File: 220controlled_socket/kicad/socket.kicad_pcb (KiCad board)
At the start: 2 copper layers, 71 parts, among them J1 DB9_Female, J2 USB_B, J3 5Vext, J4 SWIM, J5 DB15_Male, J6 Power, J7 Power, K1 SRD-05VDC, K2 SRD-05VDC, Q1 2N7002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

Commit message: 220v socket schematic is over
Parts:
- added REF**: VIA, my_footprints:VIA, F.Cu at (68.6, 73.7)
- added REF**: VIA, my_footprints:VIA, F.Cu at (57.1, 88.0)
- added REF**: VIA, my_footprints:VIA, F.Cu at (50.2, 58.3)
- C11, D5, Q6, Q8, Q9, R10, R14, R16, R18, R20, R22, R9, U10, U6, U7: moved to B.Cu
- C12: footprint Capacitor_SMD:C_0805_2012Metric_Pad1.15x1.50mm_HandSolder -> Capacitor_SMD:C_0603_1608Metric_Pad0.84x1.00mm_HandSolder; moved to B.Cu
- R15, R17: value 100 -> 150
- R19, R21: footprint Resistor_SMD:R_1206_3216Metric_Pad1.24x1.80mm_HandSolder -> Resistor_THT:R_Axial_DIN0309_L9.0mm_D3.2mm_P12.70mm_Horizontal
- R24: footprint Resistor_SMD:R_0603_1608Metric_Pad0.84x1.00mm_HandSolder -> Resistor_SMD:R_0805_2012Metric_Pad1.15x1.50mm_HandSolder
- REF** (x4): footprint MountingHole:MountingHole_3.2mm_M3 -> my_footprints:Hole_3mm
- moved C6 181.8 mm to (54.7, 62.4)
- moved R15 174.8 mm to (64.9, 25.1), turned to 180 degrees
- moved R8 173.2 mm to (68.2, 88.5), turned to 90 degrees
- moved R18 166.5 mm to (77.1, 53.4), turned to 180 degrees
- moved R16 166.3 mm to (81.7, 28.2), turned to 180 degrees
- moved Q2 161.7 mm to (61.5, 87.0)
- moved R3 156.8 mm to (61.0, 83.8)
- moved U6 154.9 mm to (66.0, 82.9)
- moved U5 151.5 mm to (78.9, 84.5), turned to 90 degrees
- moved Q1 150.1 mm to (67.6, 76.6), turned to 180 degrees
- moved Q8 149.7 mm to (87.0, 27.4)
- moved R5 149.4 mm to (57.3, 36.6), turned to 270 degrees
- moved R10 145.4 mm to (79.2, 87.4), turned to 180 degrees
- moved R17 145.2 mm to (77.1, 53.5), turned to 180 degrees
- moved Q4 144.6 mm to (94.1, 84.6)
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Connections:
- K1 pad 2: Net-(K1-Pad2) -> VCC
- K1 pad 3: (no net) -> Net-(D3-Pad1)
- K1 pad 4: Net-(D3-Pad1) -> (no net)
- K1 pad 5: VCC -> Net-(K1-Pad5)
- K2 pad 2: Net-(K2-Pad2) -> VCC
- K2 pad 3: (no net) -> Net-(D4-Pad1)
- K2 pad 4: Net-(D4-Pad1) -> (no net)
- K2 pad 5: VCC -> Net-(K2-Pad5)
- Q8 pad 3: Net-(K1-Pad2) -> Net-(K1-Pad5)
- Q9 pad 3: Net-(K2-Pad2) -> Net-(K2-Pad5)
- R10 pad 1: Net-(J5-Pad10) -> Net-(J5-Pad9)
- U10 pad 1: Net-(J6-Pad3) -> Net-(D3-Pad1)
- U10 pad 2: Net-(J6-Pad3) -> Net-(D3-Pad1)
- U10 pad 3: Net-(D3-Pad1) -> Net-(J6-Pad3)
- U10 pad 4: Net-(D3-Pad1) -> Net-(J6-Pad3)
- U3 pad 10: /PKEY1 -> /Out0
- U3 pad 11: /Out1 -> /PKEY1
- U3 pad 12: /Out0 -> /~In0
- U3 pad 14: Net-(C13-Pad1) -> /Relay1
- U3 pad 16: /Relay1 -> /Triac1
- U3 pad 17: /Triac1 -> /Relay0
- U3 pad 19: /Relay0 -> /Triac0
- U3 pad 20: /Triac0 -> Net-(C13-Pad1)
- U3 pad 5: /~In0 -> /~In1
- U3 pad 6: /~In1 -> /Out1
- U5 pad 2: Net-(J5-Pad9) -> Net-(J5-Pad10)
- U5 pad 3: GND -> /~In1
- U5 pad 4: /~In1 -> GND
- U6 pad 3: Net-(J5-Pad3) -> Net-(J5-Pad4)
- U6 pad 4: Net-(J5-Pad4) -> Net-(J5-Pad3)
- U7 pad 3: Net-(J5-Pad1) -> Net-(J5-Pad2)
- U7 pad 4: Net-(J5-Pad2) -> Net-(J5-Pad1)
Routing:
- net GND: track 21.9 -> 513.2 mm, vias 0 -> 5
- net VCC: track 16.0 -> 197.0 mm, vias 0 -> 2
- net /NKEY2: track 0.00 -> 65.0 mm
- net /NKEY1: track 0.00 -> 63.7 mm
- net /PKEY1: track 0.00 -> 62.7 mm, vias 0 -> 1
- net /Cur0: track 0.00 -> 60.9 mm, vias 0 -> 1
- net /~In0: track 6.73 -> 63.1 mm, vias 0 -> 1
- net /Out0: track 0.00 -> 48.4 mm
- net /~In1: track 5.73 -> 53.4 mm, vias 0 -> 1
- net GNDREF: track 0.00 -> 46.8 mm
- net Net-(R17-Pad1): track 0.00 -> 45.2 mm, vias 0 -> 1
- net Net-(D4-Pad1): track 0.00 -> 44.5 mm
- net /Out1: track 0.00 -> 42.9 mm
- net Net-(D3-Pad2): track 0.00 -> 42.8 mm
- net Net-(R15-Pad1): track 0.00 -> 40.5 mm, vias 0 -> 1
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- added copper zone on B.Cu, net GND
- added copper zone on F.Cu, net GND
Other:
- board outline added: 87 x 71 mm

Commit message: fix error in U5 connection on 220v socket
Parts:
- U5: moved to B.Cu
- moved U5 2.54 mm to (81.4, 84.5)
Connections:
- U5 pad 1: Net-(R10-Pad2) -> Net-(J5-Pad10)
- U5 pad 2: Net-(J5-Pad10) -> Net-(R10-Pad2)
- U5 pad 3: /~In1 -> GND
- U5 pad 4: GND -> /~In1
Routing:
- net GND: track 513.2 -> 518.8 mm

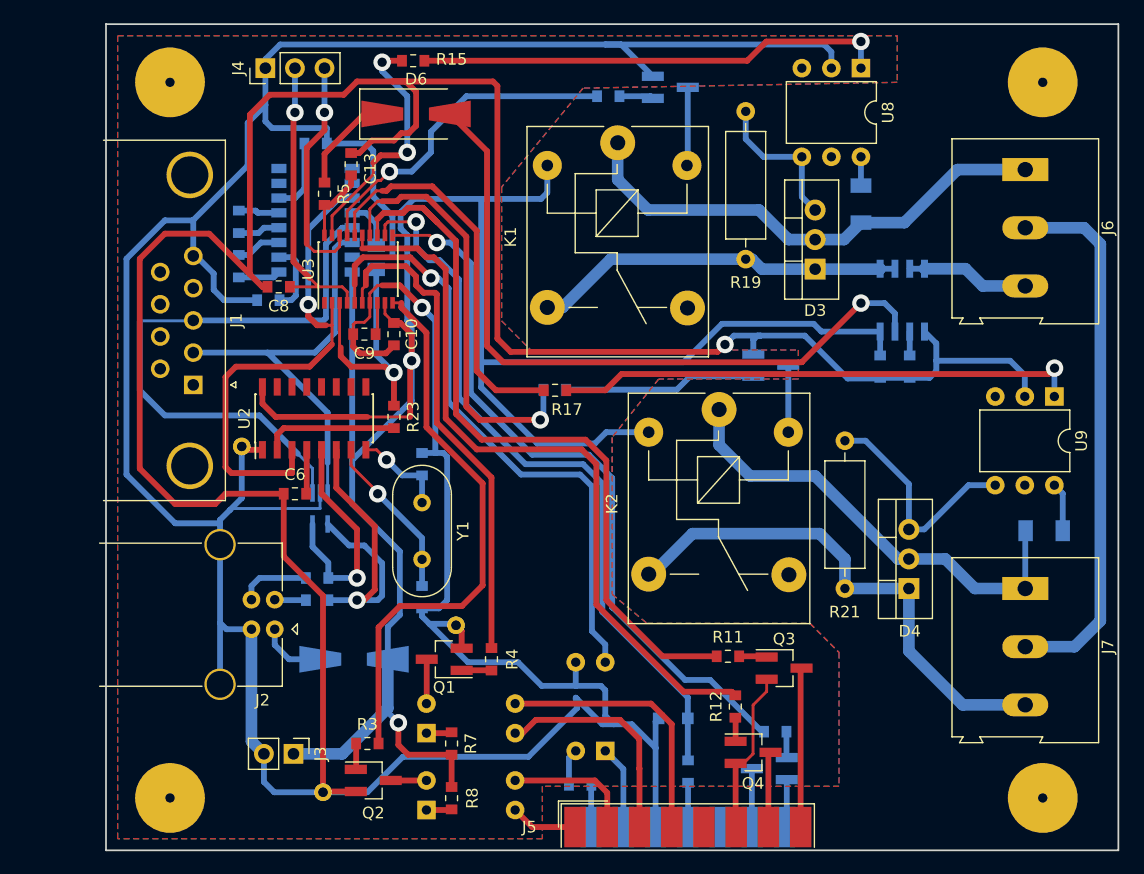
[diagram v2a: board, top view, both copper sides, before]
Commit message: fix bugs in 220v socket schematics
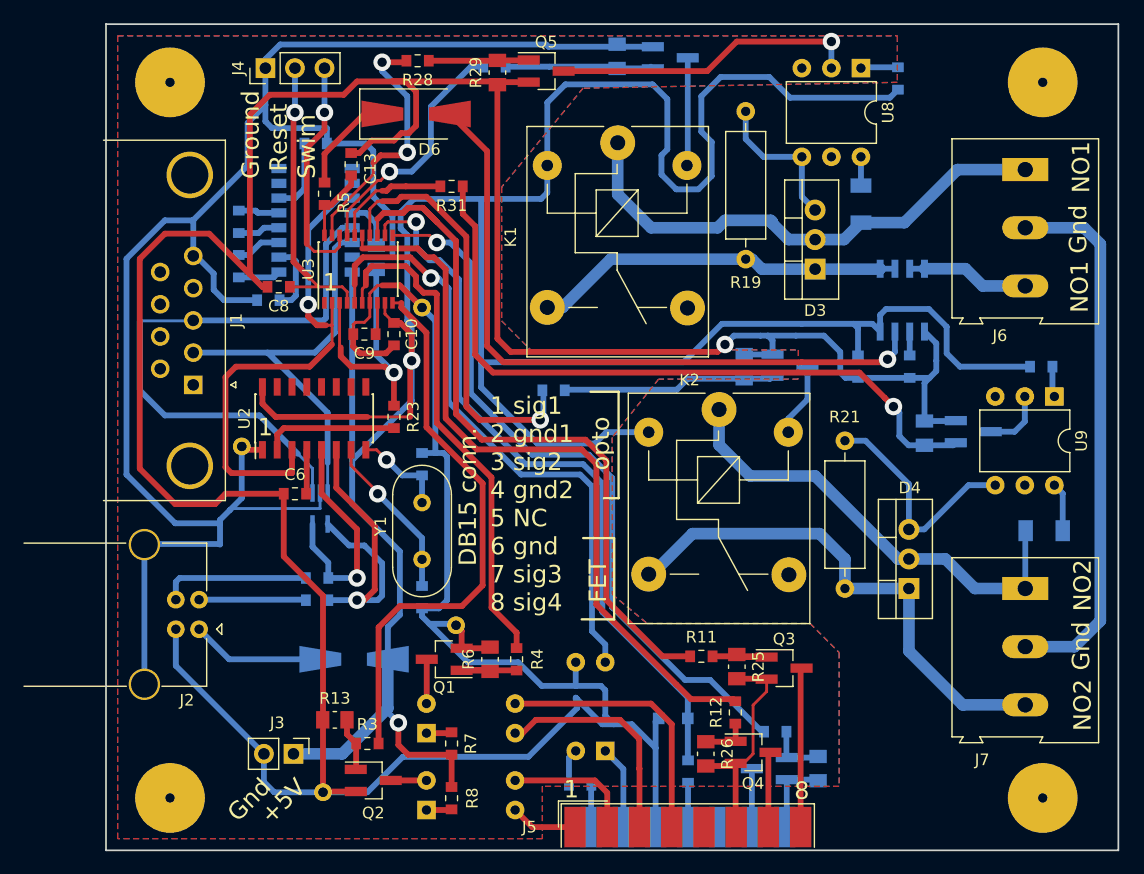
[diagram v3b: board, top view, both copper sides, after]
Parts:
- added Q5: 2N7002, Package_TO_SOT_SMD:SOT-23_Handsoldering, F.Cu at (76.3, 26.0)
- added Q7: 2N7002, Package_TO_SOT_SMD:SOT-23_Handsoldering, B.Cu at (113.0, 57.0)
- added R13: 47k, Resistor_SMD:R_0805_2012Metric_Pad1.15x1.50mm_HandSolder, F.Cu at (58.2, 81.8)
- added R25: 47k, Resistor_SMD:R_0805_2012Metric_Pad1.15x1.50mm_HandSolder, F.Cu at (92.7, 77.2)
- added R26: 47k, Resistor_SMD:R_0805_2012Metric_Pad1.15x1.50mm_HandSolder, F.Cu at (90.0, 84.7)
- added R27: 47k, Resistor_SMD:R_0805_2012Metric_Pad1.15x1.50mm_HandSolder, B.Cu at (99.7, 86.0)
- added R28: 330, Resistor_SMD:R_0603_1608Metric_Pad0.84x1.00mm_HandSolder, F.Cu at (65.3, 25.1)
- added R29: 47k, Resistor_SMD:R_0805_2012Metric_Pad1.15x1.50mm_HandSolder, F.Cu at (72.1, 26.2)
- added R30: 47k, Resistor_SMD:R_0805_2012Metric_Pad1.15x1.50mm_HandSolder, B.Cu at (82.4, 24.8)
- added R31: 330, Resistor_SMD:R_0603_1608Metric_Pad0.84x1.00mm_HandSolder, F.Cu at (68.2, 35.9)
- added R32: 47k, Resistor_SMD:R_0805_2012Metric_Pad1.15x1.50mm_HandSolder, B.Cu at (108.8, 57.1)
- added R33: 47k, Resistor_SMD:R_0805_2012Metric_Pad1.15x1.50mm_HandSolder, B.Cu at (93.3, 51.4)
- added R6: 47k, Resistor_SMD:R_0805_2012Metric_Pad1.15x1.50mm_HandSolder, F.Cu at (71.5, 76.6)
- added REF**: VIA, my_footprints:VIA, F.Cu at (65.7, 46.4)
- R15, R17: moved to B.Cu
- moved R17 41.8 mm to (118.9, 51.4)
- moved R15 41.7 mm to (106.6, 26.7), turned to 270 degrees
- moved R16 10.1 mm to (71.9, 25.7)
- moved J2 6.50 mm to (46.5, 74.0)
- moved Q8 2.54 mm to (87.0, 24.9)
- moved R11 2.29 mm to (89.7, 76.3)
- moved R4 2.16 mm to (73.8, 76.6)
- moved C11 1.91 mm to (103.1, 51.4)
- moved Q9 1.65 mm to (97.3, 51.3)
- moved R12 0.51 mm to (92.6, 81.2)
- moved R18 0.10 mm to (77.0, 53.5)
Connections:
- J5 pad 6: Net-(J5-Pad6) -> GND
- Q3 pad 2: Net-(J5-Pad6) -> GND
- Q4 pad 2: Net-(J5-Pad6) -> GND
- R15 pad 2: /Triac0 -> VCC
- R17 pad 2: /Triac1 -> VCC
- U8 pad 2: GND -> Net-(Q5-Pad3)
- U9 pad 2: GND -> Net-(Q7-Pad3)
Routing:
- net VCC: track 197.0 -> 270.7 mm
- net Net-(Q7-Pad1): track 0.00 -> 60.7 mm, vias 0 -> 1
- net Net-(R17-Pad1): track 45.2 -> 2.63 mm, vias 1 -> 0
- net Net-(R15-Pad1): track 40.5 -> 3.21 mm, vias 1 -> 0
- net Net-(Q5-Pad3): track 0.00 -> 26.3 mm, vias 0 -> 1
- net /Triac1: track 33.5 -> 10.3 mm
- net Net-(J5-Pad6): track 14.2 -> 0.00 mm
- net Net-(Q8-Pad1): track 2.95 -> 13.0 mm
- net GND: track 518.8 -> 527.6 mm
- net Net-(Q5-Pad1): track 0.00 -> 8.61 mm
- net /Relay0: track 28.7 -> 21.2 mm
- net Net-(J2-Pad3): track 6.14 -> 12.8 mm
- net Net-(J2-Pad2): track 2.70 -> 9.20 mm
- net Net-(D2-Pad2): track 5.78 -> 11.5 mm
- net Net-(Q7-Pad3): track 0.00 -> 5.44 mm
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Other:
- board text added: "+5V"
- board text added: "1"
- board text added: "1 sig1 2 gnd1 3 sig2 4 gnd2 5 NC 6 gnd 7 sig3 8 sig4"
- board text added: "15"
- board text added: "8"
- board text added: "9"
- board text added: "9 +5v1 10 gnd1 11 gnd 12 3..5V log.in 13 NC 14 gnd2 15 3..15V"
- board text added: "DB15 conn."
- board text added: "FET"
- board text added: "Gnd"
- board text added: "Ground"
- board text added: "NO1"
- board text added: "NO2"
- board text added: "PMOS"
- board text added: "Reset"
- board text added: "Swim"
- board text added: "opto"

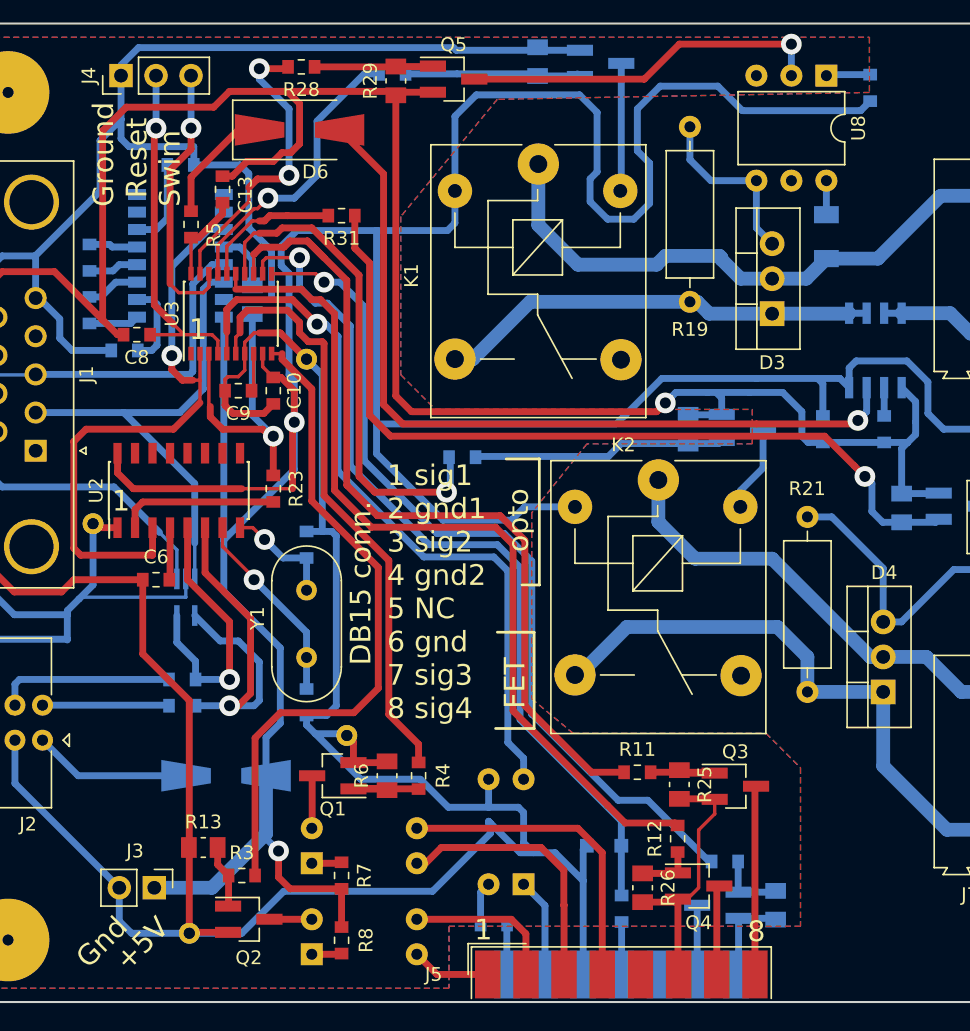
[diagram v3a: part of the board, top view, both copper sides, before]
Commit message: fix bug in max3232 & ch340 connection
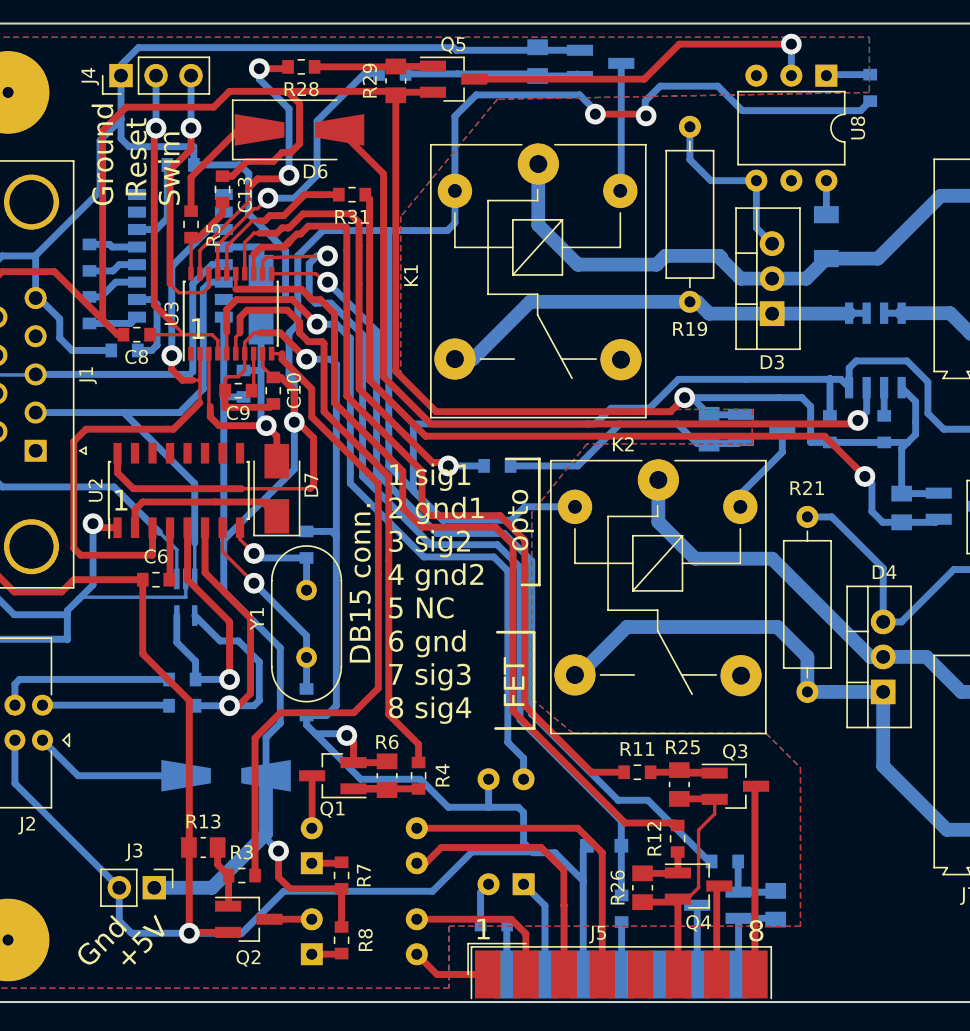
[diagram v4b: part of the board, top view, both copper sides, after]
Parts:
- removed R24: 510, Resistor_SMD:R_0805_2012Metric_Pad1.15x1.50mm_HandSolder
- removed the REF** at (65.7, 46.4)
- removed the REF** at (57.1, 88.0)
- removed the REF** at (50.2, 58.3)
- removed the REF** at (68.6, 73.7)
- added D7: SS14, Diode_SMD:D_SMA, F.Cu at (63.5, 55.8)
- added D8: SS14, Diode_SMD:D_SMA, B.Cu at (62.4, 42.0)
- R23: value 510 -> 4k7; moved to B.Cu
- moved R23 7.92 mm to (61.1, 48.1)
- moved R18 2.62 mm to (79.5, 54.1)
- moved R31 1.70 mm to (69.0, 34.4)
- moved R33 1.52 mm to (94.9, 51.4)
- moved Q9 1.40 mm to (98.7, 51.3)
- moved C11 0.51 mm to (103.6, 51.4)
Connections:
- R23 pad 1: Net-(R23-Pad1) -> VCC
- U2 pad 2: Net-(R23-Pad1) -> Net-(D7-Pad1)
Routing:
- net Net-(D7-Pad1): track 0.00 -> 12.3 mm
- net Net-(R23-Pad1): track 11.6 -> 0.00 mm
- net VCC: track 270.7 -> 262.3 mm, vias 2 -> 4
- net /~In0: track 63.1 -> 66.0 mm
- net /NKEY1: track 63.9 -> 61.7 mm
- net /Relay1: track 36.6 -> 35.1 mm
- net /Triac1: track 10.3 -> 11.7 mm
- net /Cur0: track 59.0 -> 57.8 mm
- net /Rx: track 22.1 -> 21.1 mm
- net /PKEY1: track 62.7 -> 62.1 mm
- net Net-(K2-Pad5): track 6.45 -> 7.03 mm
- net /NKEY2: track 62.7 -> 62.2 mm
- net Net-(C5-Pad2): track 8.08 -> 8.58 mm

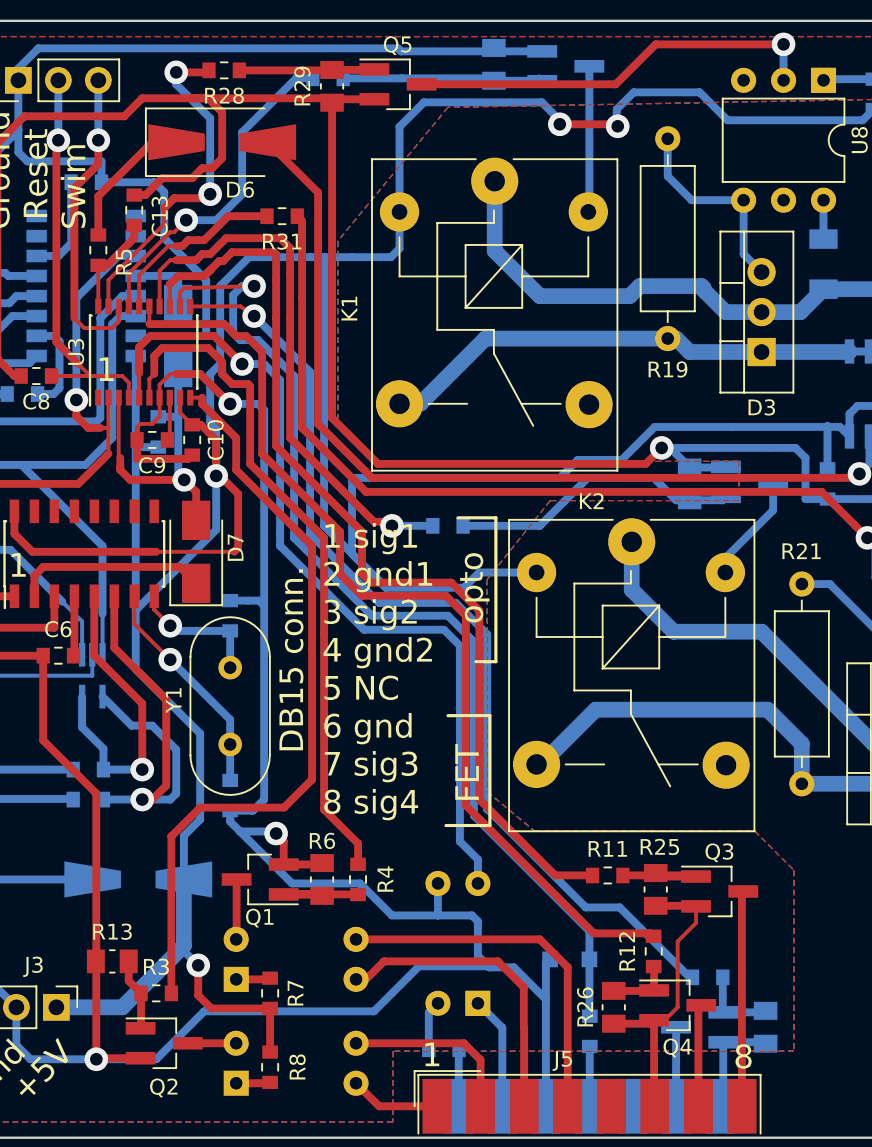
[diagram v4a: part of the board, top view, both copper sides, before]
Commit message: fix PCB 220v socket
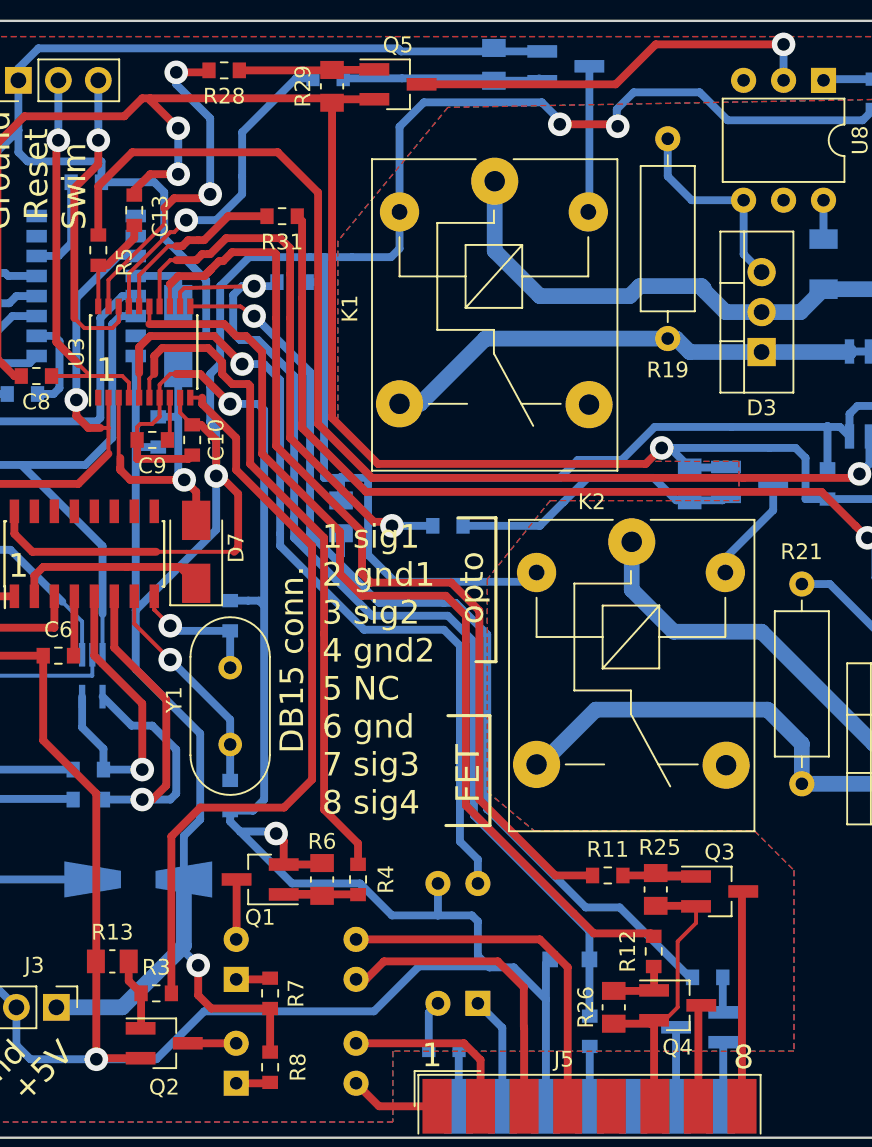
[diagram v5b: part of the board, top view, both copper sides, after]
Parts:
- removed D6: SS14, Diode_SMD:D_SMA-SMB_Universal_Handsoldering
- added R24: 4k7, Resistor_SMD:R_0603_1608Metric_Pad0.84x1.00mm_HandSolder, B.Cu at (69.6, 38.6)
- D5: value MM3Z3V6 -> 5V suppressor
- moved R27 42.2 mm to (72.7, 53.5)
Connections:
- R27 pad 1: Net-(J5-Pad15) -> /PKEY1
- R27 pad 2: Net-(Q6-Pad1) -> VCC
- R5 pad 1: Net-(D6-Pad1) -> /Cur0
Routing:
- net /Cur0: track 57.8 -> 72.3 mm
- net Net-(D6-Pad1): track 8.86 -> 0.00 mm
- net VCC: track 262.3 -> 256.8 mm
- net GND: track 527.4 -> 524.6 mm, vias 5 -> 7
- net Net-(Q6-Pad1): track 4.97 -> 2.24 mm
- net Net-(J5-Pad15): track 6.88 -> 4.15 mm
- net /PKEY1: track 62.1 -> 63.9 mm
- net /~In0: track 66.0 -> 67.6 mm
